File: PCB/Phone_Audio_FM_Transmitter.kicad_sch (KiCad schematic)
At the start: 32 parts, among them J1 Vin, J2 Conn_Coaxial, J3 Conn_Coaxial, J4 USB_B_Micro, J6 Rec, J7 Trans, U1 TPS5403, U2 Si4706, U3 Si4711, U4 ESP32-S3-WROOM-1

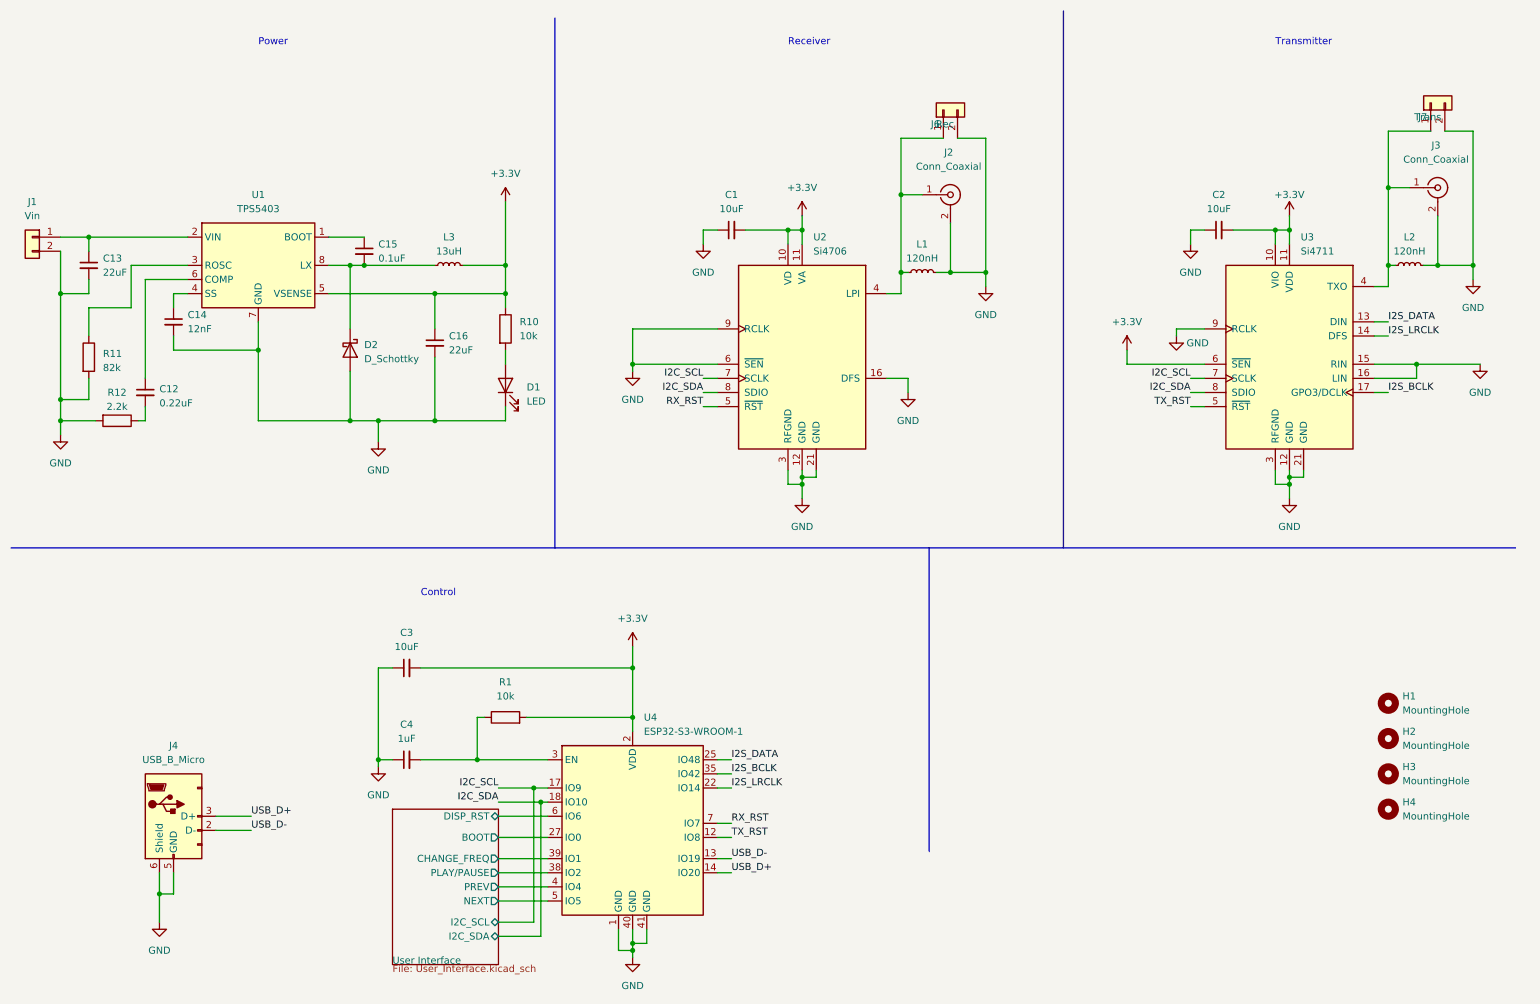
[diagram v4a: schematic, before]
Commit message: Changed microcontroller from ESP32-S3 to ESP32 and added UART bridge
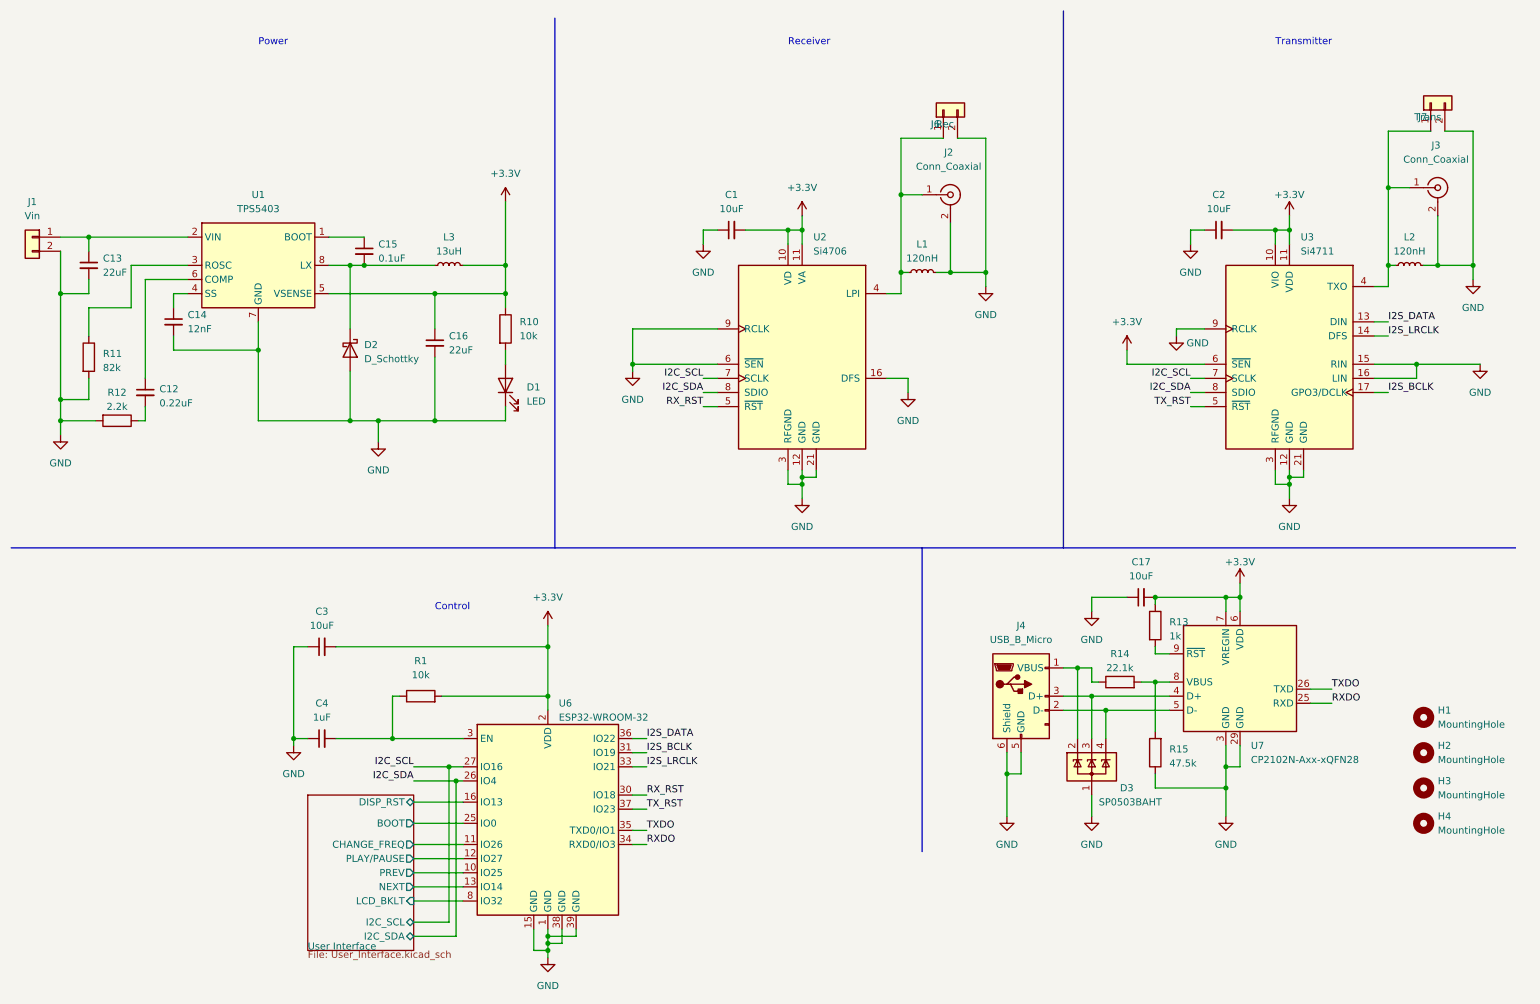
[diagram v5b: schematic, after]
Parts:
- removed U4: ESP32-S3-WROOM-1, RF_Module:ESP32-S3-WROOM-1, symbol RF_Module:ESP32-WROOM-32
- added C17: 10uF, Capacitor_SMD:C_0805_2012Metric_Pad1.18x1.45mm_HandSolder, symbol Device:C_Small
- added D3: SP0503BAHT, Package_TO_SOT_SMD:SOT-143, symbol Power_Protection:SP0503BAHT
- added R13: 1k, Resistor_SMD:R_0805_2012Metric_Pad1.20x1.40mm_HandSolder, symbol Device:R
- added R14: 22.1k, Resistor_SMD:R_0805_2012Metric_Pad1.20x1.40mm_HandSolder, symbol Device:R
- added R15: 47.5k, Resistor_SMD:R_0805_2012Metric_Pad1.20x1.40mm_HandSolder, symbol Device:R
- added U6: ESP32-WROOM-32, RF_Module:ESP32-WROOM-32, symbol RF_Module:ESP32-WROOM-32
- added U7: CP2102N-Axx-xQFN28, Package_DFN_QFN:QFN-28-1EP_5x5mm_P0.5mm_EP3.35x3.35mm, symbol Interface_USB:CP2102N-Axx-xQFN28
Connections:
- net +3.3V: now also C17.2, R13.1, U6.2 (VDD), U7.6 (VDD), U7.7 (VREGIN)
- net GND: now also C17.1, D3.1 (A), R15.1, U6.1 (GND), U6.15 (GND), U6.38 (GND), U6.39 (GND), U7.29 (GND), U7.3 (GND)
- net I2C_SCL: now also U6.27 (IO16)
- net I2C_SDA: now also U6.26 (IO4)
- net I2S_BCLK: now also U6.31 (IO19)
- net I2S_DATA: now also U6.36 (IO22)
- net I2S_LRCLK: now also U6.33 (IO21)
- net RX_RST: now also U6.30 (IO18)
- net TX_RST: now also U6.37 (IO23)
- net User Interface/BOOT: now also U6.25 (IO0)
- net User Interface/CHANGE_FREQ: now also U6.11 (IO26)
- net User Interface/DISP_RST: now also U6.16 (IO13)
- net User Interface/NEXT: now also U6.13 (IO14)
- net User Interface/PLAY/PAUSE: now also U6.12 (IO27)
- net User Interface/PREV: now also U6.10 (IO25)
- net at C4.2, R1.1: now also U6.3 (EN)
- net at J4.1 (VBUS): now also D3.2 (K), R14.1
- net USB_D+: no longer names the net of J4.3 (D+)
- net USB_D+: now also D3.3 (K), U7.4 (D+)
- net USB_D-: no longer names the net of J4.2 (D-)
- net USB_D-: now also D3.4 (K), U7.5 (D-)
- new net: R14.2, R15.2, U7.8 (VBUS)
- new net: R13.2, U7.9 (~{RST})
- new net RXDO: U6.34 (RXD0/IO3), U7.25 (RXD)
- new net TXDO: U6.35 (TXD0/IO1), U7.26 (TXD)
- new net User Interface/LCD_BKLT: U6.8 (IO32)
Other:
- sheet User Interface ports: added LCD_BKLT; removed none
- moved on the sheet: C3, C4, H1, H2, H3, H4, R1

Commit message: Completed PCB Rev 2. Changed microcontroller to ESP32-WROOM-32, added UART bridge, removed button pull-up resistors, added I2S test point, added option to control backlight, and better organized all traces
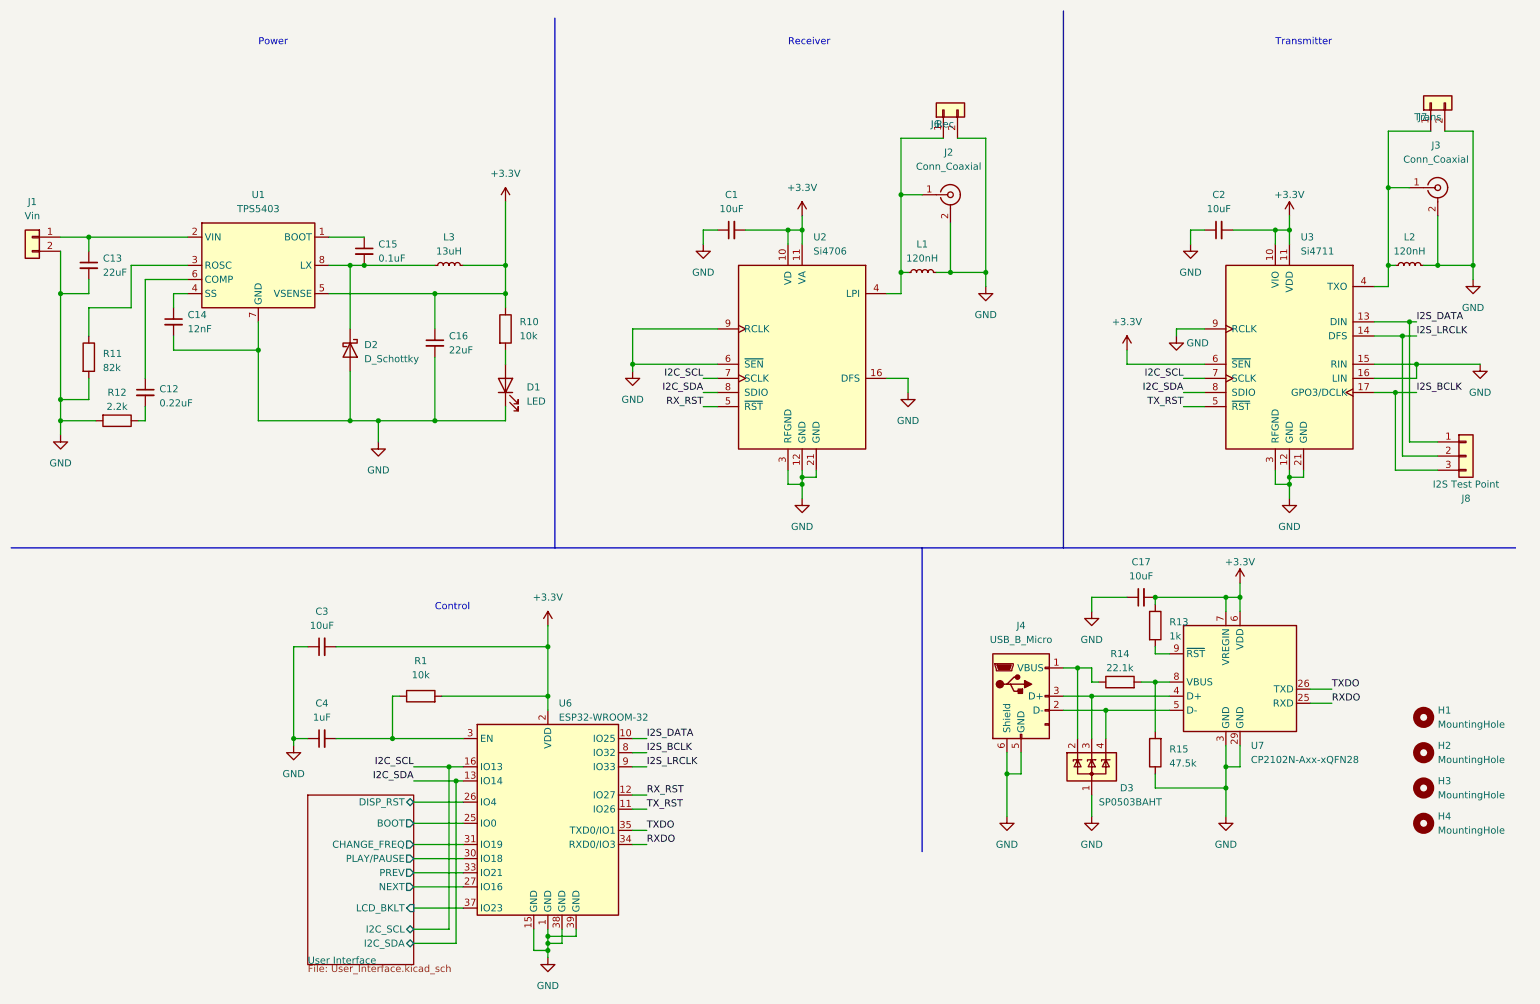
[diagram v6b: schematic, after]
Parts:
- added J8: I2S Test Point, Connector_Molex:Molex_KK-254_AE-6410-03A_1x03_P2.54mm_Vertical, symbol Connector_Generic:Conn_01x03
- D1: footprint LED_SMD:LED_0805_2012Metric_Pad1.15x1.40mm_HandSolder -> LED_SMD:LED_1206_3216Metric_Pad1.42x1.75mm_HandSolder
- D2: footprint Diode_SMD:D_0805_2012Metric_Pad1.15x1.40mm_HandSolder -> Diode_SMD:D_1206_3216Metric_Pad1.42x1.75mm_HandSolder
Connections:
- net I2C_SCL: now also U6.16 (IO13); no longer U6.27 (IO16)
- net I2C_SDA: now also U6.13 (IO14); no longer U6.26 (IO4)
- net I2S_BCLK: now also U6.8 (IO32), J8.3 (Pin_3); no longer U6.31 (IO19)
- net I2S_DATA: now also U6.10 (IO25), J8.1 (Pin_1); no longer U6.36 (IO22)
- net I2S_LRCLK: now also U6.9 (IO33), J8.2 (Pin_2); no longer U6.33 (IO21)
- net RX_RST: now also U6.12 (IO27); no longer U6.30 (IO18)
- net TX_RST: now also U6.11 (IO26); no longer U6.37 (IO23)
- net User Interface/CHANGE_FREQ: now also U6.31 (IO19); no longer U6.11 (IO26)
- net User Interface/DISP_RST: now also U6.26 (IO4); no longer U6.16 (IO13)
- net User Interface/LCD_BKLT: now also U6.37 (IO23); no longer U6.8 (IO32)
- net User Interface/NEXT: now also U6.27 (IO16); no longer U6.13 (IO14)
- net User Interface/PLAY/PAUSE: now also U6.30 (IO18); no longer U6.12 (IO27)
- net User Interface/PREV: now also U6.33 (IO21); no longer U6.10 (IO25)

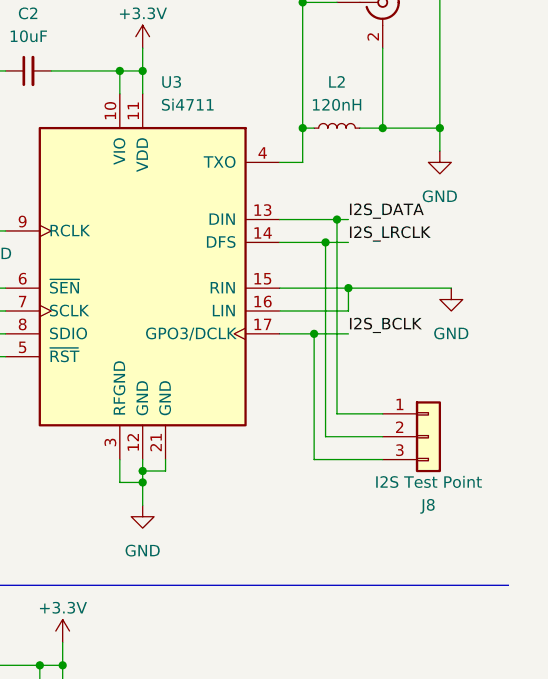
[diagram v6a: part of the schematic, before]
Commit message: Added resistors to I2S pins on transmitter
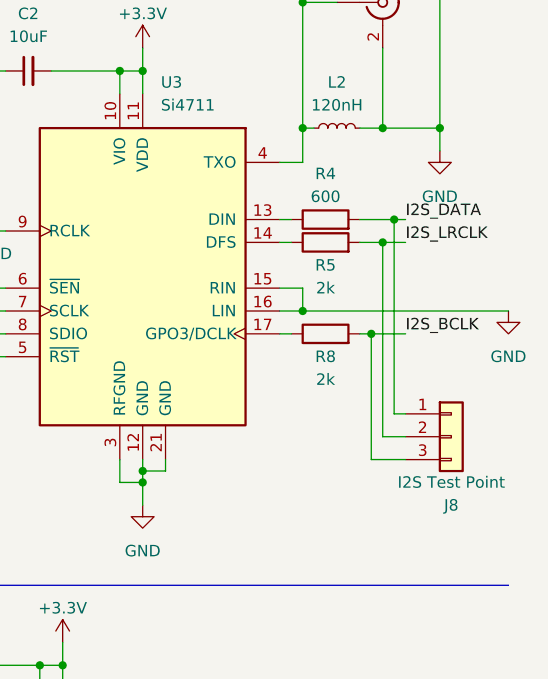
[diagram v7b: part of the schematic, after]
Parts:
- added R4: 600, Resistor_SMD:R_0805_2012Metric_Pad1.20x1.40mm_HandSolder, symbol Device:R
- added R5, R8: 2k, Resistor_SMD:R_0805_2012Metric_Pad1.20x1.40mm_HandSolder, symbol Device:R
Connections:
- net I2S_BCLK: now also R8.2; no longer U3.17 (GPO3/DCLK)
- net I2S_DATA: now also R4.2; no longer U3.13 (DIN)
- net I2S_LRCLK: now also R5.2; no longer U3.14 (DFS)
- new net: R8.1, U3.17 (GPO3/DCLK)
- new net: R4.1, U3.13 (DIN)
- new net: R5.1, U3.14 (DFS)
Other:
- moved on the sheet: J8

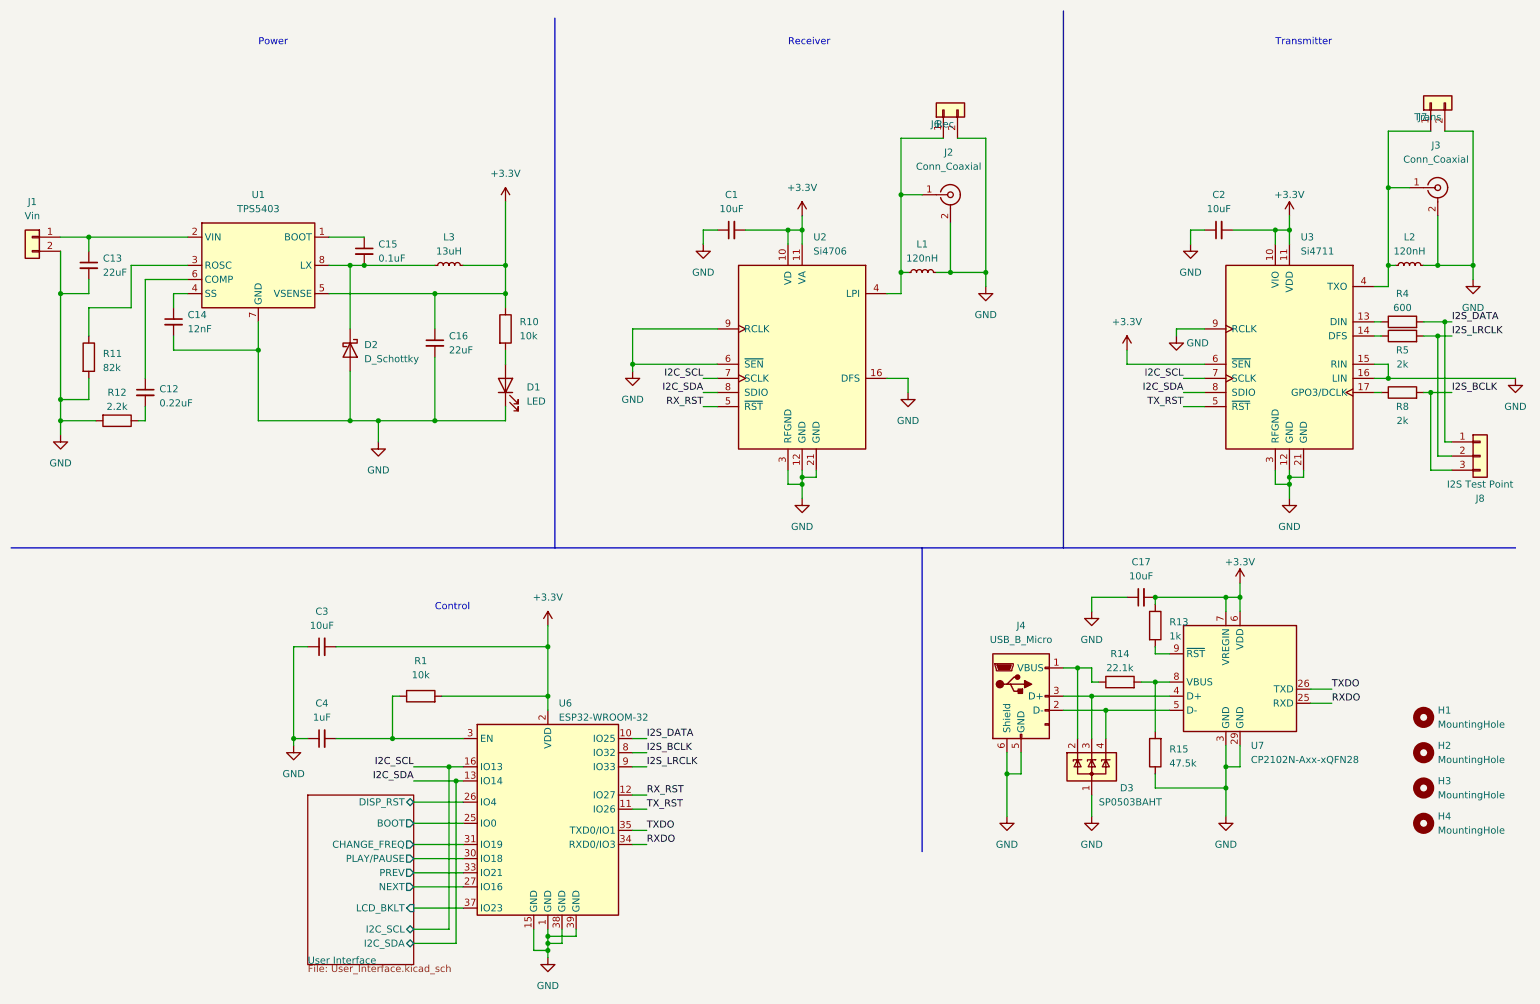
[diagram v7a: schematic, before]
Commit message: Added crystal oscillator for receiver IC and RCLK from ESP32 to FM ICs
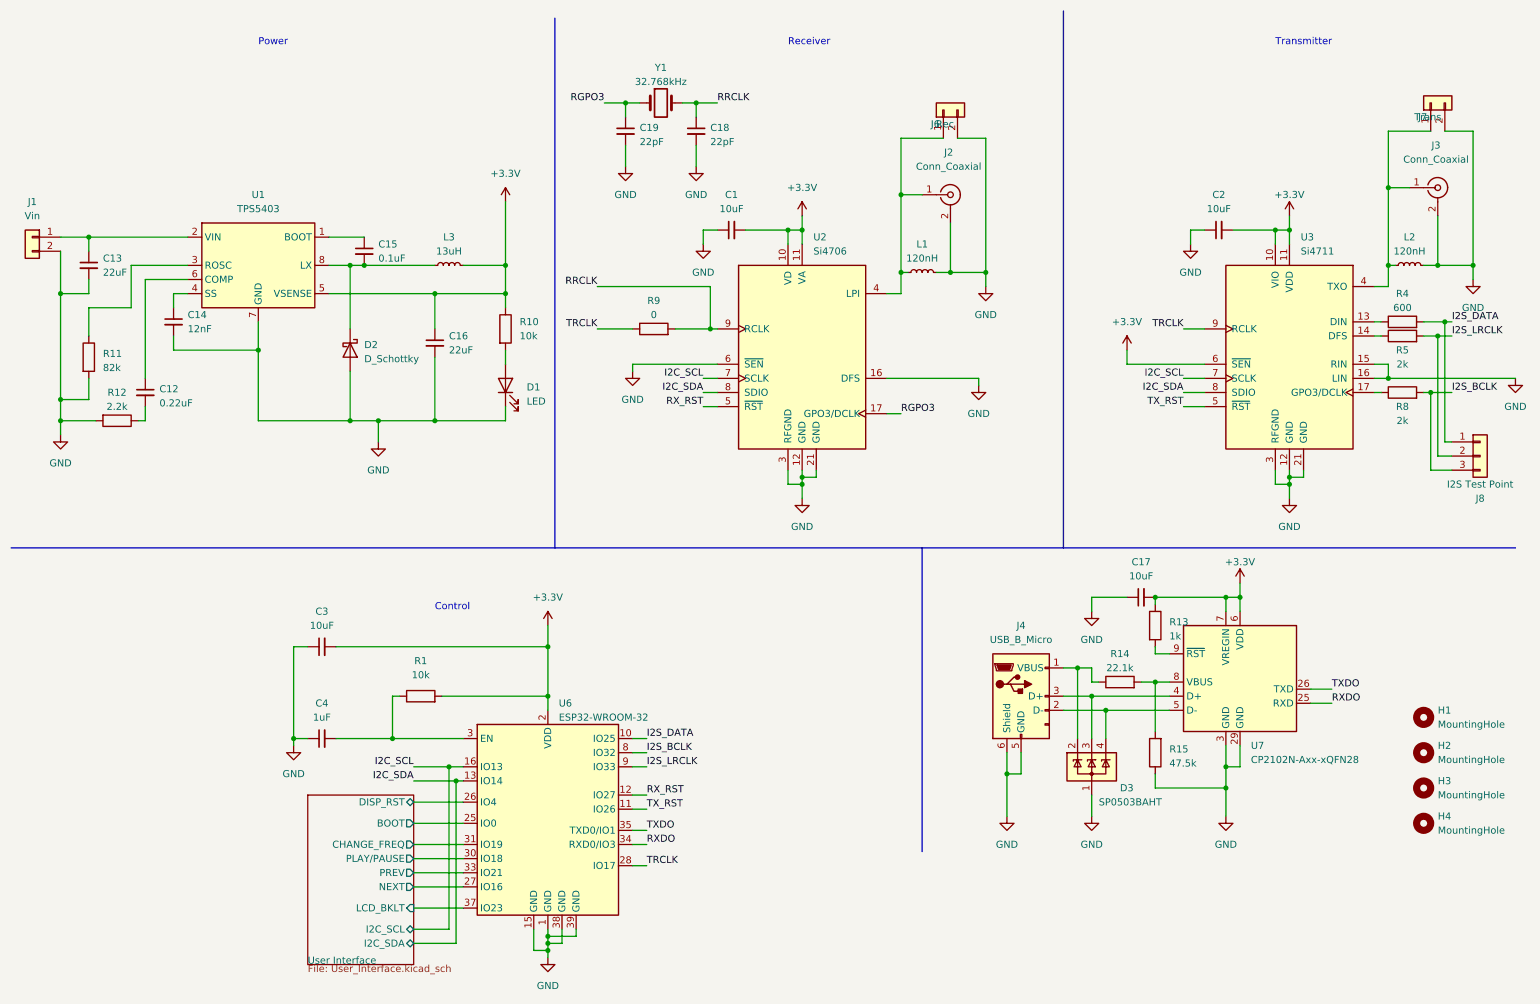
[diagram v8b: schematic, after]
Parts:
- added C18, C19: 22pF, Capacitor_SMD:C_0805_2012Metric_Pad1.18x1.45mm_HandSolder, symbol Device:C_Small
- added R9: 0, Resistor_SMD:R_0805_2012Metric_Pad1.20x1.40mm_HandSolder, symbol Device:R
- added Y1: 32.768kHz, Crystal:Crystal_SMD_2012-2Pin_2.0x1.2mm_HandSoldering, symbol Device:Crystal
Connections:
- net GND: now also C18.2, C19.2; no longer U2.9 (RCLK), U3.9 (RCLK)
- net RGPO3: now reaches U2.17 (GPO3/DCLK)
- net RGPO3: now also C19.1, Y1.1
- net TRCLK: now reaches U6.28 (IO17)
- net TRCLK: now also U3.9 (RCLK), R9.1
- new net RRCLK: C18.1, R9.2, U2.9 (RCLK), Y1.2
